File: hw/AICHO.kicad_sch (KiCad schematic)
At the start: 77 parts, among them J1 Conn_01x06, J101 Conn_01x03, J102 Conn_01x02, J103 Conn_01x02, J104 Conn_01x02, J201 Conn_01x03, J202 Conn_01x02, J203 Conn_01x02, J204 Conn_01x02, J21 Conn_01x02, J22 Conn_01x02, J3 USB_A, J301 Conn_01x03, J302 Conn_01x02, J303 Conn_01x02, J304 Conn_01x02, J4 AudioJack3_SwitchTR, J401 Conn_01x03, J402 Conn_01x02, J403 Conn_01x02, J404 Conn_01x02, J5 Speaker, Q1 Si2302, Q10 Si2302, Q11 Si2302, Q12 Si2302, Q2 Si2302, Q3 Si2302, Q4 Si2302, Q5 Si2302, Q6 Si2302, Q7 Si2302, Q8 Si2302, Q9 Si2302, U1 RP2040, U2 W25Q128JVPIQ, U3 SPX3819M5-L-3-3, U4 USBLC6-2SC6, U5 MAX98357AETE+, U6 SN74AHCT245PWR, Y1 12MHz

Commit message: 🚧 Revise schematic
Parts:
- removed C18: 10u, Capacitor_SMD:C_0603_1608Metric, symbol Device:C
- removed R6: 100k, Resistor_SMD:R_0603_1608Metric, symbol Device:R
- removed U5: MAX98357AETE+, MAX98357AETE+:QFN50P300X300X80-17N, symbol MAX98357AETE+:MAX98357AETE+
- added C18, C20, C22, C24, C36, C38, C40: 10u, Capacitor_SMD:C_0603_1608Metric, symbol Device:C_Polarized
- added C21, C23, C25, C30, C35, C37, C39, C41: 100n, Capacitor_SMD:C_0402_1005Metric, symbol Device:C
- added C26, C27, C32: 2.2u, Capacitor_SMD:C_0402_1005Metric, symbol Device:C
- added C28, C29: 2.2n, Capacitor_SMD:C_0402_1005Metric, symbol Device:C
- added C31: 1u, Capacitor_SMD:C_0402_1005Metric, symbol Device:C
- added C33, C34: 470n, Capacitor_SMD:C_0402_1005Metric, symbol Device:C
- added C42: 2.2u, symbol Device:C
- added J6: AudioJack3_SwitchTR, Connector_Audio:Jack_3.5mm_CUI_SJ1-3525N_Horizontal, symbol Connector_Audio:AudioJack3_SwitchTR
- added R10: 2.2k, symbol Device:R
- added R11: 150k, symbol Device:R
- added R12: 100k, symbol Device:R
- added R8, R9: 470, Resistor_SMD:R_0603_1608Metric, symbol Device:R
- added U5: PCM5102A, Package_SO:TSSOP-20_4.4x6.5mm_P0.65mm, symbol Audio:PCM5102A
- added U6: OPA1622, Package_SON:Texas_S-PVSON-N10, symbol Amplifier_Audio:OPA1622
- added U7: MAX9814, Package_DFN_QFN:DFN-14-1EP_3x3mm_P0.4mm_EP1.78x2.35mm, symbol Amplifier_Audio:MAX9814
- added U8: PCM1808PWR, PCM1808PWR:PCM1808PWR, symbol PCM1808PWR:PCM1808PWR
- renumbered C20 to C50, J3 to J2, R7 to R6, R8 to R7, U6 to U9
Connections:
- net +3V3: now also C19.1, C18.1, C20.1, C21.1, C22.1, C23.1, C36.1, C37.1, U5.1 (CPVDD), U5.17 (XSMT), U5.20 (DVDD), U5.8 (AVDD), U8.10 (MD0), U8.11 (MD1), U8.12 (FMT), U8.4 (VDD)
- net +5V: now also C30.1, C31.1, C38.1, C39.1, U6.2 (V+), U6.8 (EN), U7.5 (VDD), U8.3 (VCC); no longer C19.1
- net AUDIO_SPEAKER+: now also J4.TN; no longer J4.RN
- net GND: now also C18.2, C20.2, C21.2, C22.2, C23.2, C24.2, C25.2, C27.2, C28.2, C29.2, C30.2, C31.2, C32.2, C33.2, C34.2, C36.2, C37.2, C38.2, C39.2, C40.2, C41.2, J6.S, R12.1, U5.10 (DEMP), U5.11 (FLT), U5.16 (FMT), U5.19 (DGND), U5.3 (CPGND), U5.9 (AGND), U6.11 (V-), U6.3 (GND), U6.4 (V-), U7.11 (GND), U7.15 (GND), U7.4 (GND), U7.7 (GND), U7.9 (A/R), U8.2 (AGND), U8.5 (DGND)
- net I2S_CK: now also U5.13 (BCK)
- net I2S_SD: now also U5.14 (DIN)
- net I2S_WS: now also U5.15 (LRCK)
- net AUDIO_OUT+ renamed AUDIO_OUT_L
- net AUDIO_OUT_L: now also U6.10 (-), U6.9; no longer J4.R
- net AUDIO_OUT- renamed AUDIO_OUT_COM
- new net: C34.1, U7.1 (CT)
- new net: C42.1, U8.13 (VINL), U8.14 (VINR)
- new net: R10.2, R11.1, R12.2, U7.13 (MICBIAS)
- new net: C24.1, C25.1, U5.18 (LDOO)
- new net: C26.1, U5.2 (CAPP)
- new net: C26.2, U5.4 (CAPM)
- new net: C27.1, U5.5 (VNEG)
- new net: R8.1, U5.6 (OUTL)
- new net: R9.1, U5.7 (OUTR)
- new net: C40.1, C41.1, U8.1 (VREF)
- new net: C33.1, U7.12 (BIAS)
- new net: R11.2, U7.14 (TH)
- new net: C32.1, U7.3 (CG)
- new net: C35.2, U7.8 (MICIN)
- new net AUDIO_OUT_R: J4.R, U6.6 (-), U6.7
- new net LINE_OUT_L: C28.1, R8.2, U6.1 (+)
- new net LINE_OUT_R: C29.1, R9.2, U6.5 (+)
- new net MIC_ADC_CK: U8.8 (BCK)
- new net MIC_ADC_SCK: U8.6 (SCKI)
- new net MIC_ADC_SD: U8.9 (DOUT)
- new net MIC_ADC_WS: U8.7 (LRCK)
- new net MIC_IN: C35.1, J6.T, R10.1
- new net MIC_OUT: C42.2, U7.6 (MICOUT)
- new net MIC_SHDN: U7.2 (~{SHDN})
- no-connect marks 16 -> 17
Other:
- note added: "AGND"
- note added: "AVDD/AGND"
- note added: "CPGND"
- note added: "CPVDD/CPGND"
- note added: "DGND"
- note added: "DVDD/DGND"
- note added: "Left-justified"
- note added: "Master mode, 256 f_s"
- note added: "VCC/AGND"
- note added: "VDD/DGND"
- note removed: "+3 dB gain"
- note removed: "Not shut down Selected channel: L"
- moved on the sheet: J4, J5

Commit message: 🚧 Update layout
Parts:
- added C43: 2.2n, Capacitor_SMD:C_0402_1005Metric, symbol Device:C
- added R13: 470, Resistor_SMD:R_0402_1005Metric, symbol Device:R
- C42: footprint (none) -> Capacitor_SMD:C_0402_1005Metric
- R10, R11, R12: footprint (none) -> Resistor_SMD:R_0402_1005Metric
- R8, R9: footprint Resistor_SMD:R_0603_1608Metric -> Resistor_SMD:R_0402_1005Metric
- renumbered C50 to C45
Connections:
- net AUDIO_OUT_COM is gone; now on net GND: J4.S, J5.2
- net ACT1: now also U1.37 (GPIO25); no longer U1.34 (GPIO22)
- net ACT2: now also U1.38 (GPIO26_ADC0); no longer U1.35 (GPIO23)
- net AUDIO_OUT_L: now also U6.6 (-), U6.7; no longer U6.10 (-), U6.9
- net AUDIO_OUT_R: now also U6.10 (-), U6.9; no longer U6.6 (-), U6.7
- net GND: now also C43.2
- net I2S_CK: now also U1.4 (GPIO2); no longer U1.5 (GPIO3)
- net I2S_SD: now also U1.3 (GPIO1); no longer U1.4 (GPIO2)
- net I2S_WS: now also U1.5 (GPIO3); no longer U1.6 (GPIO4)
- net LINE_OUT_L: now also U6.5 (+); no longer U6.1 (+)
- net LINE_OUT_R: now also U6.1 (+); no longer U6.5 (+)
- net MIC_ADC_CK: now also U1.7 (GPIO5)
- net MIC_ADC_SCK: now also U1.9 (GPIO7)
- net MIC_ADC_SD: now also U1.6 (GPIO4)
- net MIC_ADC_WS: now also U1.8 (GPIO6)
- net MIC_SHDN: now also U1.11 (GPIO8)
- net ORG1_LED: now also U1.29 (GPIO18); no longer U1.14 (GPIO11)
- net ORG1_PUMP_DRAIN: now also U1.15 (GPIO12); no longer U1.9 (GPIO7)
- net ORG1_PUMP_INFLATE: now also U1.14 (GPIO11); no longer U1.8 (GPIO6)
- net ORG1_SOLENOID: now also U1.13 (GPIO10); no longer U1.7 (GPIO5)
- net ORG2_LED: now also U1.30 (GPIO19); no longer U1.15 (GPIO12)
- net ORG2_PUMP_DRAIN: now also U1.18 (GPIO15); no longer U1.13 (GPIO10)
- net ORG2_PUMP_INFLATE: now also U1.17 (GPIO14); no longer U1.12 (GPIO9)
- net ORG2_SOLENOID: now also U1.16 (GPIO13); no longer U1.11 (GPIO8)
- net ORG3_LED: now also U1.31 (GPIO20); no longer U1.16 (GPIO13)
- net ORG3_PUMP_DRAIN: now also U1.36 (GPIO24); no longer U1.31 (GPIO20)
- net ORG3_PUMP_INFLATE: now also U1.35 (GPIO23); no longer U1.30 (GPIO19)
- net ORG3_SOLENOID: now also U1.34 (GPIO22); no longer U1.29 (GPIO18)
- net ORG4_LED: now also U1.32 (GPIO21); no longer U1.17 (GPIO14)
- net at U8.13 (VINL), U8.14 (VINR): now also C43.1, R13.1; no longer C42.1
- new net: C42.1, R13.2
- no-connect marks 17 -> 12
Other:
- note added: "Audio Input"
- note added: "Cutoff 154 kHz"
- note added: "Electrolytic outperforms, but anyway"
- moved on the sheet: C31, C32, C33, C34, C35, C36, C37, C38, C39, C40, C41, C42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

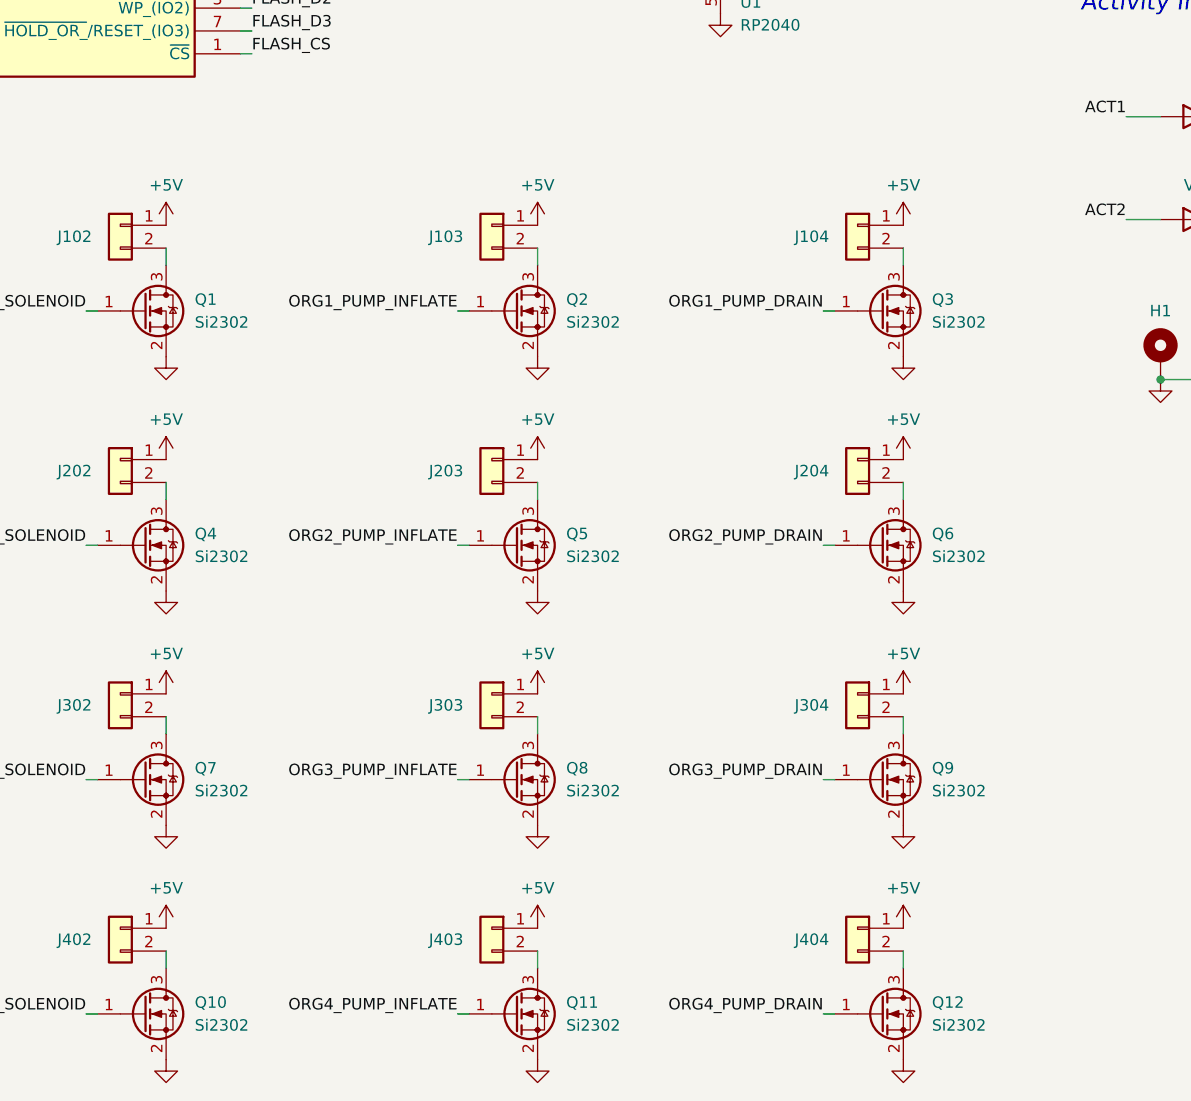
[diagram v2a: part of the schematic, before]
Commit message: Finish updated board layout & routing
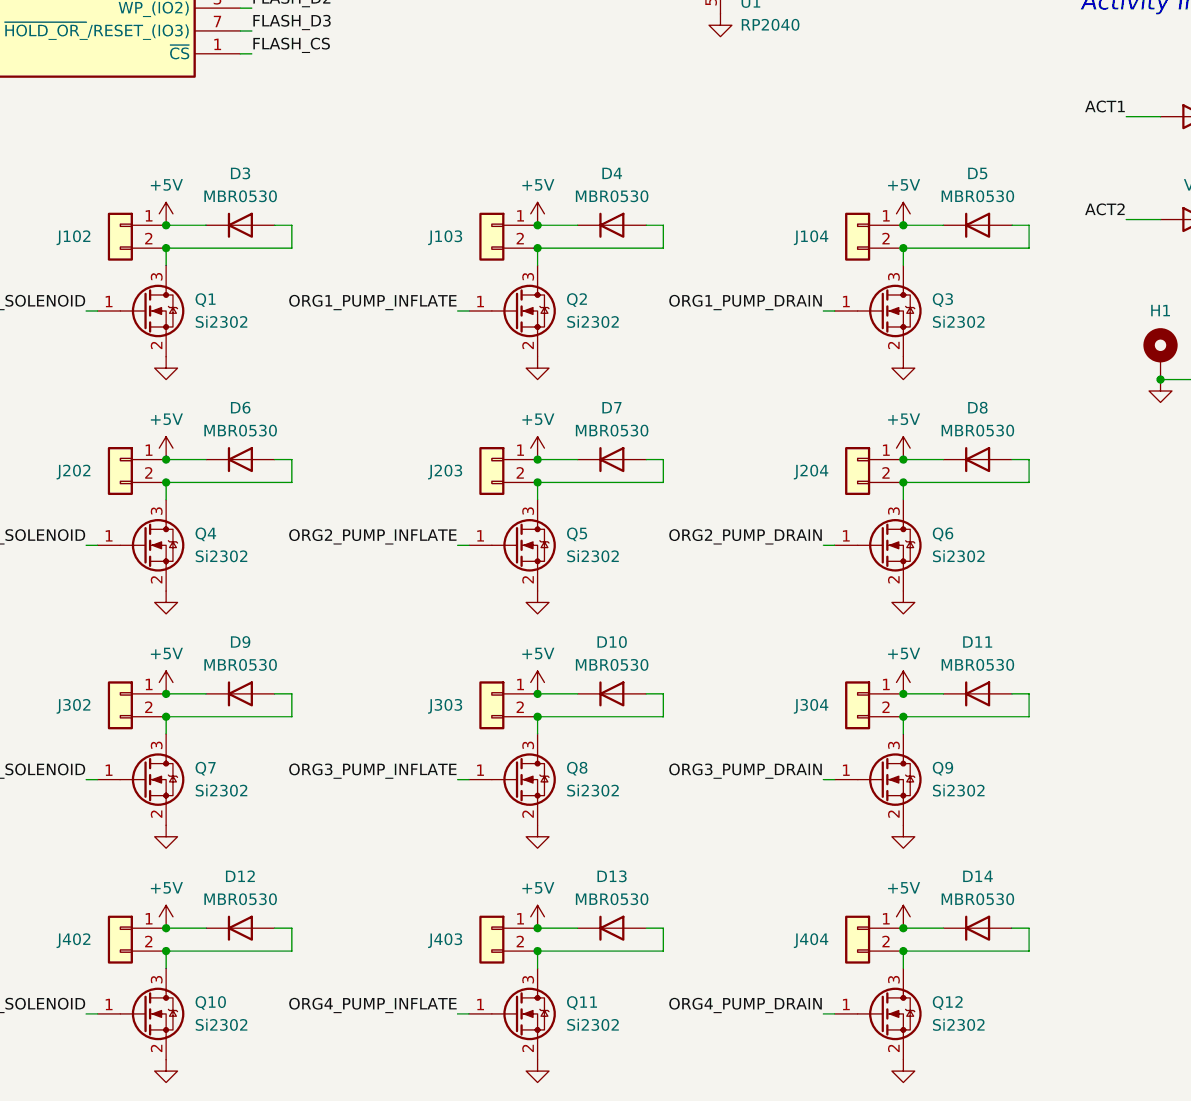
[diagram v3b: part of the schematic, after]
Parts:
- added D10, D11, D12, D13, D14, D3, D4, D5, D6, D7, D8, D9: MBR0530, Diode_SMD:D_SOD-123, symbol Device:D
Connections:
- net +5V: now also D10.1 (K), D11.1 (K), D12.1 (K), D13.1 (K), D14.1 (K), D3.1 (K), D4.1 (K), D5.1 (K), D6.1 (K), D7.1 (K), D8.1 (K), D9.1 (K)
- net at J303.2 (Pin_2), Q8.3 (D): now also D10.2 (A)
- net at J404.2 (Pin_2), Q12.3 (D): now also D14.2 (A)
- net at J403.2 (Pin_2), Q11.3 (D): now also D13.2 (A)
- net at J402.2 (Pin_2), Q10.3 (D): now also D12.2 (A)
- net at J104.2 (Pin_2), Q3.3 (D): now also D5.2 (A)
- net at J302.2 (Pin_2), Q7.3 (D): now also D9.2 (A)
- net at J304.2 (Pin_2), Q9.3 (D): now also D11.2 (A)
- net at J103.2 (Pin_2), Q2.3 (D): now also D4.2 (A)
- net at J202.2 (Pin_2), Q4.3 (D): now also D6.2 (A)
- net at J204.2 (Pin_2), Q6.3 (D): now also D8.2 (A)
- net at J102.2 (Pin_2), Q1.3 (D): now also D3.2 (A)
- net at J203.2 (Pin_2), Q5.3 (D): now also D7.2 (A)

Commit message: Clean-ups
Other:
- note added: "** This is wrong. ** R12 should be across GND and TH so as to form a resistor divider from MICBIAS"
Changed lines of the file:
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@@
+    (effects (font (size 1.27 1.27) italic) (justify left bottom))
+  )
+  (text "** This is wrong. **\nR12 should be across\nGND and TH so as to\nform a resistor divider\nfrom MICBIAS"
+    (at 262.255 145.415 0)
     (effects (font (size 1.27 1.27) italic) (justify left bottom))
   )
